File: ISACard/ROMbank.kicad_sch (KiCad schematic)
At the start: 20 parts, among them U10 28C256, U6 74LS86, U7 74LS86, U8 74LS32, U9 74LS32

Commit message: Fixed some problems with the card...
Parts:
- removed JP16: A7, Connector_PinHeader_2.54mm:PinHeader_1x02_P2.54mm_Vertical, symbol Jumper:Jumper_2_Open
- removed R16: 10k, Resistor_THT:R_Axial_DIN0207_L6.3mm_D2.5mm_P7.62mm_Horizontal, symbol Device:R
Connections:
- net A12: no longer U7.1
- net A13: now also U7.1; no longer U7.4
- net GND: now also U7.4, U7.5, U9.10, U9.9; no longer U8.12, U8.13
- net at U9.2: now also U7.11; no longer U7.6
- net at U7.2: now also JP15.2 (B), R15.2
- net at JP17.2 (C): now also U9.4; no longer U9.10
- net at U9.8: no longer U9.13
- net at U9.6: now also U9.13; no longer U9.9
- net at U8.11: now also U9.12
- net at U8.8: now also U8.12; no longer U9.12
- new net AEN: U8.13
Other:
- moved on the sheet: JP17, JP19, U6E, U7A, U7B, U7E, U8D, U8E, U9A, U9B, U9C, U9D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

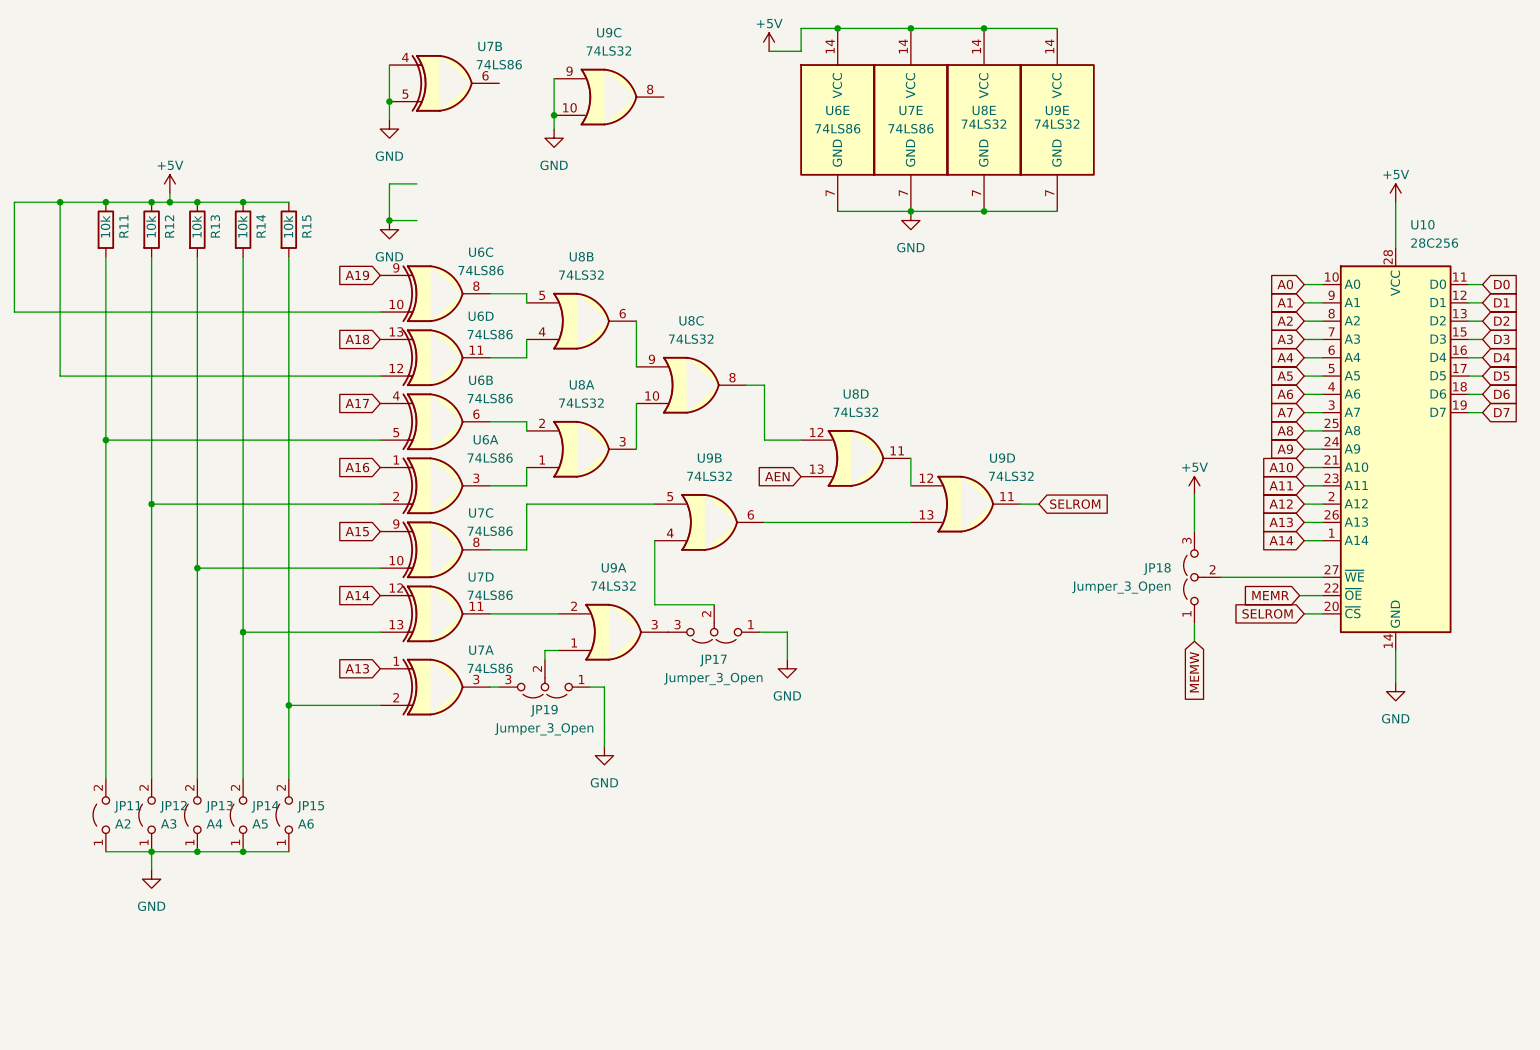
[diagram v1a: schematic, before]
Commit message: Rearranged the order of the logic
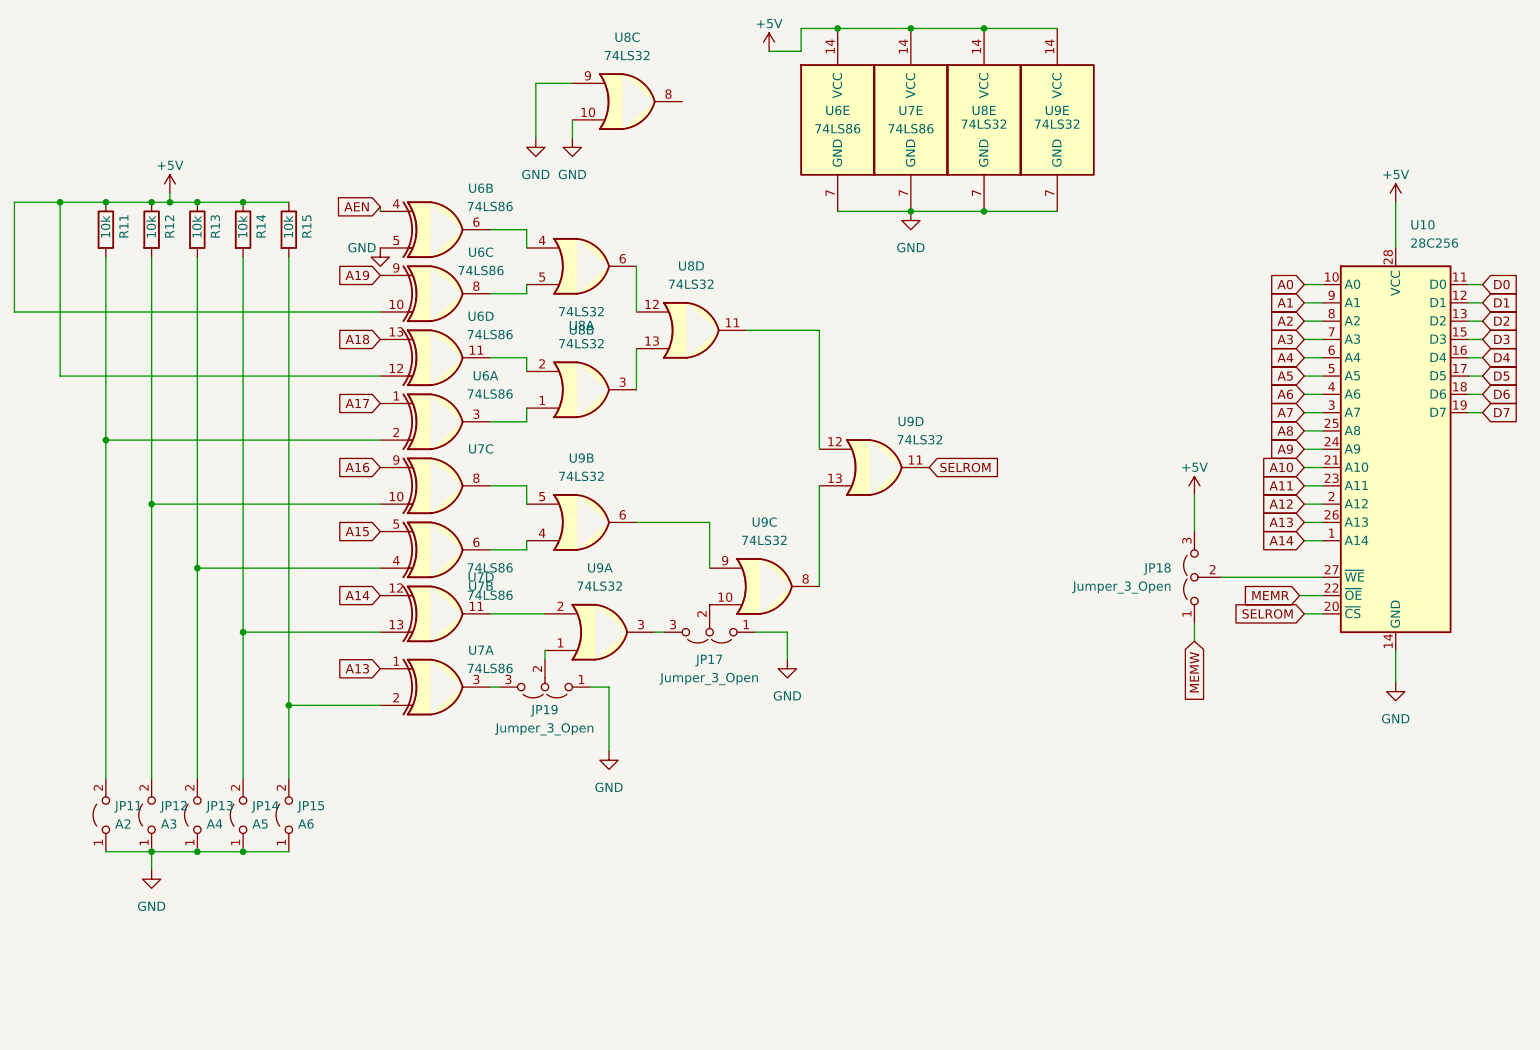
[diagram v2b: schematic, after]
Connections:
- net A15: now also U7.5; no longer U7.9
- net A16: now also U7.9; no longer U6.1
- net A17: now also U6.1; no longer U6.4
- net AEN: now also U6.4; no longer U8.13
- net GND: now also U6.5, U8.10, U8.9; no longer U7.4, U7.5, U9.10, U9.9
- net at U9.8: now also U9.13
- net at JP13.2 (B), R13.2: now also U7.4; no longer U7.10
- net at JP11.2 (B), R11.2: now also U6.2; no longer U6.5
- net at U8.2: now also U6.11; no longer U6.6
- net at U8.3: now also U8.13; no longer U8.10
- net at JP12.2 (B), R12.2: now also U7.10; no longer U6.2
- net at U8.4: now also U6.6; no longer U6.11
- net at U8.6: now also U8.12; no longer U8.9
- net at U8.8: no longer U8.12
- net at U9.6: now also U9.9; no longer U9.13
- net at JP17.2 (C): now also U9.10; no longer U9.4
- net at U7.6: now also U9.4
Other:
- moved on the sheet: JP17, U6A, U6B, U7B, U7C, U8A, U8B, U8C, U8D, U9A, U9B, U9C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

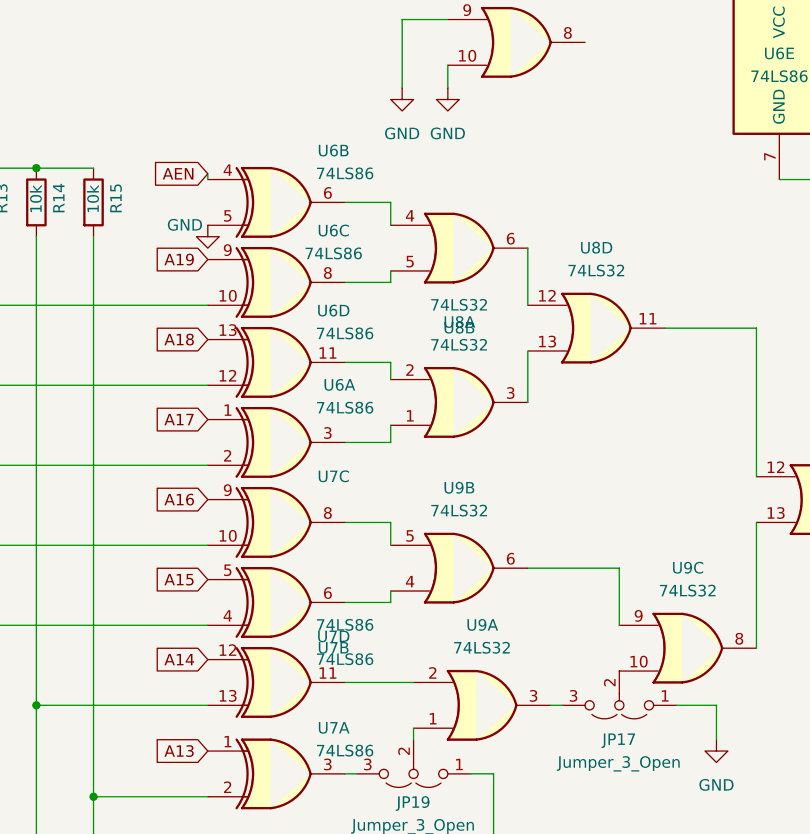
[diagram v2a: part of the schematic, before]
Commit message: fixed rom labels
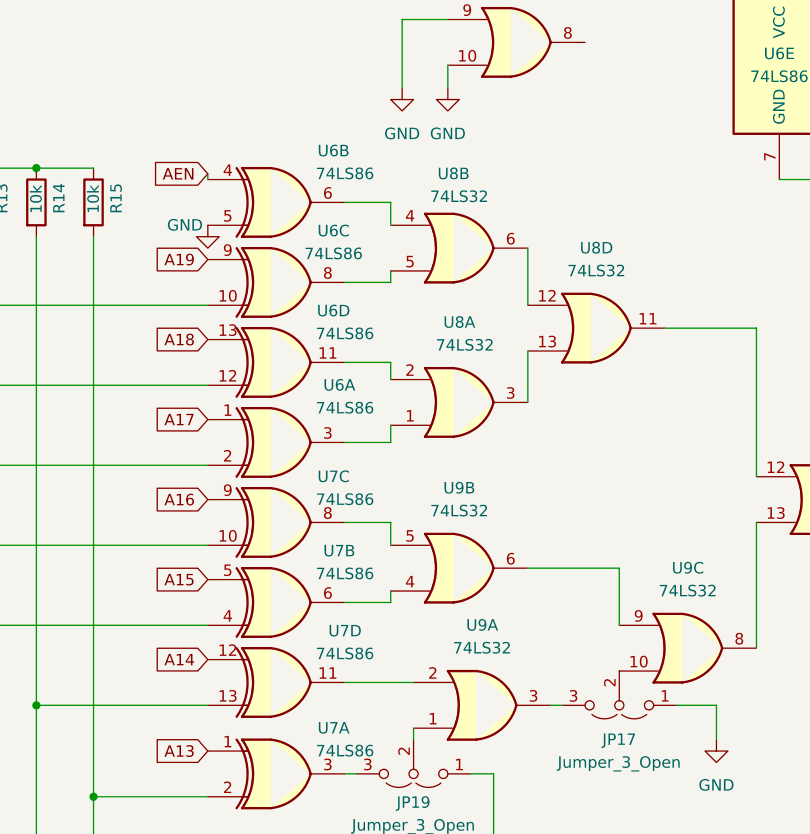
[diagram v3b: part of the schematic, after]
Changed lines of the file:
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@@
     )
     (property "Value" "74LS86" (at 118.11 97.79 0)
-      (effects (font (size 1.27 1.27)) hide)
+      (effects (font (size 1.27 1.27)))
     )
     (property "Footprint" "Package_DIP:DIP-14_W7.62mm_Socket" (at 110.49 100.33 0)
@@
       (effects (font (size 1.27 1.27)))
     )
-    (property "Value" "74LS32" (at 130.81 80.645 0)
+    (property "Value" "74LS32" (at 131.445 80.645 0)
       (effects (font (size 1.27 1.27)))
     )
@@
   (symbol (lib_id "74xx:74LS32") (at 130.81 69.85 0) (unit 2)
     (in_bom yes) (on_board yes) (dnp no)
-    (property "Reference" "U8" (at 130.81 78.74 0)
-      (effects (font (size 1.27 1.27)))
-    )
-    (property "Value" "74LS32" (at 130.81 76.2 0)
+    (property "Reference" "U8" (at 130.175 61.595 0)
+      (effects (font (size 1.27 1.27)))
+    )
+    (property "Value" "74LS32" (at 130.81 64.135 0)
       (effects (font (size 1.27 1.27)))
     )
@@
   (symbol (lib_id "74xx:74LS86") (at 110.49 118.11 0) (unit 4)
     (in_bom yes) (on_board yes) (dnp no)
-    (property "Reference" "U7" (at 116.84 113.03 0)
-      (effects (font (size 1.27 1.27)))
-    )
-    (property "Value" "74LS86" (at 118.11 115.57 0)
+    (property "Reference" "U7" (at 118.11 112.395 0)
+      (effects (font (size 1.27 1.27)))
+    )
+    (property "Value" "74LS86" (at 118.11 114.935 0)
       (effects (font (size 1.27 1.27)))
     )
@@
   (symbol (lib_id "74xx:74LS86") (at 110.49 109.22 0) (mirror x) (unit 2)
     (in_bom yes) (on_board yes) (dnp no)
-    (property "Reference" "U7" (at 116.84 114.3 0)
-      (effects (font (size 1.27 1.27)))
-    )
-    (property "Value" "74LS86" (at 118.11 111.76 0)
-      (effects (font (size 1.27 1.27)))
-    )
+    (property "Reference" "U7" (at 117.475 103.505 0)
+      (effects (font (size 1.27 1.27)))
+    )
+    (property "Value" "74LS86" (at 118.11 106.045 0)
+      (effects (font (size 1.27 1.27)))
+    )

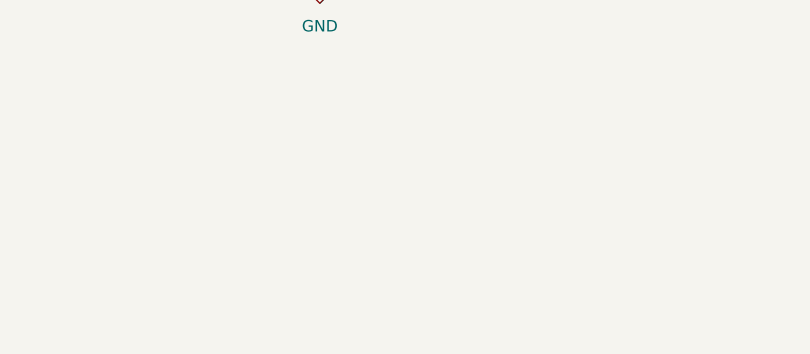
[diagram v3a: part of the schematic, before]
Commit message: moved SD card slots to edge
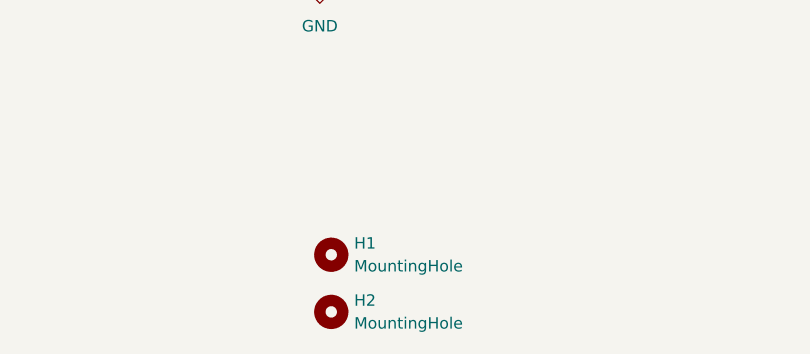
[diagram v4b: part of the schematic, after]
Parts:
- added H1, H2: MountingHole, MountingHole:MountingHole_3.7mm, symbol Mechanical:MountingHole
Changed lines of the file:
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@@
+    )
+  )
+  (symbol (lib_id "Mechanical:MountingHole") (at 135.89 167.64 0) (unit 1)
+    (in_bom yes) (on_board yes) (dnp no) (fields_autoplaced)
+    (property "Reference" "H1" (at 138.43 166.37 0)
+      (effects (font (size 1.27 1.27)) (justify left))
+    )
+    (property "Value" "MountingHole" (at 138.43 168.91 0)
+      (effects (font (size 1.27 1.27)) (justify left))
+    )
+    (property "Footprint" "MountingHole:MountingHole_3.7mm" (at 135.89 167.64 0)
+      (effects (font (size 1.27 1.27)) hide)
+    )
+    (property "Datasheet" "~" (at 135.89 167.64 0)
+      (effects (font (size 1.27 1.27)) hide)
+    )
+    (instances
+      (project "ISACard"
+        (path "/02f59ec8-9e35-4f4f-ad74-c5620a79c783/c9673afe-6a47-4001-a17b-47c886543b3d"
+          (reference "H1") (unit 1)
+        )
+      )
     )
   )
@@
         )
       )
+    )
+  )
+  (symbol (lib_id "Mechanical:MountingHole") (at 135.89 173.99 0) (unit 1)
+    (in_bom yes) (on_board yes) (dnp no) (fields_autoplaced)
+    (property "Reference" "H2" (at 138.43 172.72 0)
+      (effects (font (size 1.27 1.27)) (justify left))
+    )
+    (property "Value" "MountingHole" (at 138.43 175.26 0)
+      (effects (font (size 1.27 1.27)) (justify left))
+    )
+    (property "Footprint" "MountingHole:MountingHole_3.7mm" (at 135.89 173.99 0)
+      (effects (font (size 1.27 1.27)) hide)
+    )
+    (property "Datasheet" "~" (at 135.89 173.99 0)
+      (effects (font (size 1.27 1.27)) hide)
+    )
+    (instances
+      (project "ISACard"
+        (path "/02f59ec8-9e35-4f4f-ad74-c5620a79c783/c9673afe-6a47-4001-a17b-47c886543b3d"
+          (reference "H2") (unit 1)
+        )
+      )
